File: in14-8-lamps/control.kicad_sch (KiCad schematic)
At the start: 20 parts, among them J2 Conn_01x02_Pin, J3 Conn_01x06_Pin, Q10 2N7002, U3 ESP32-WROOM-32D, U4 DS3231M, U5 74141

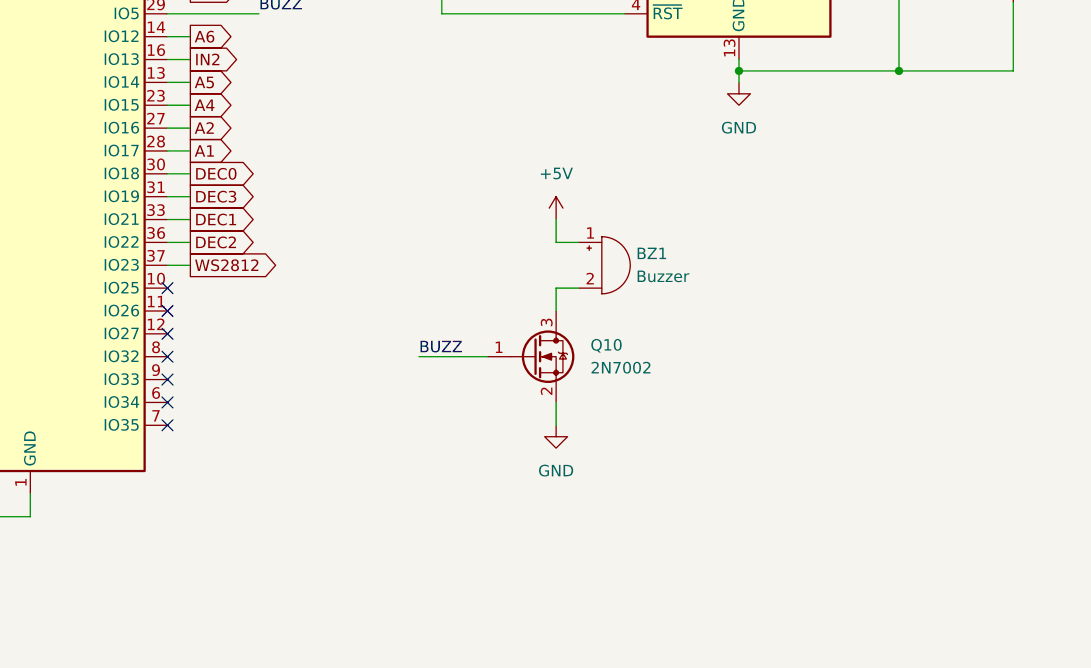
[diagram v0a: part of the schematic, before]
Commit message: add button and ws2812 connector
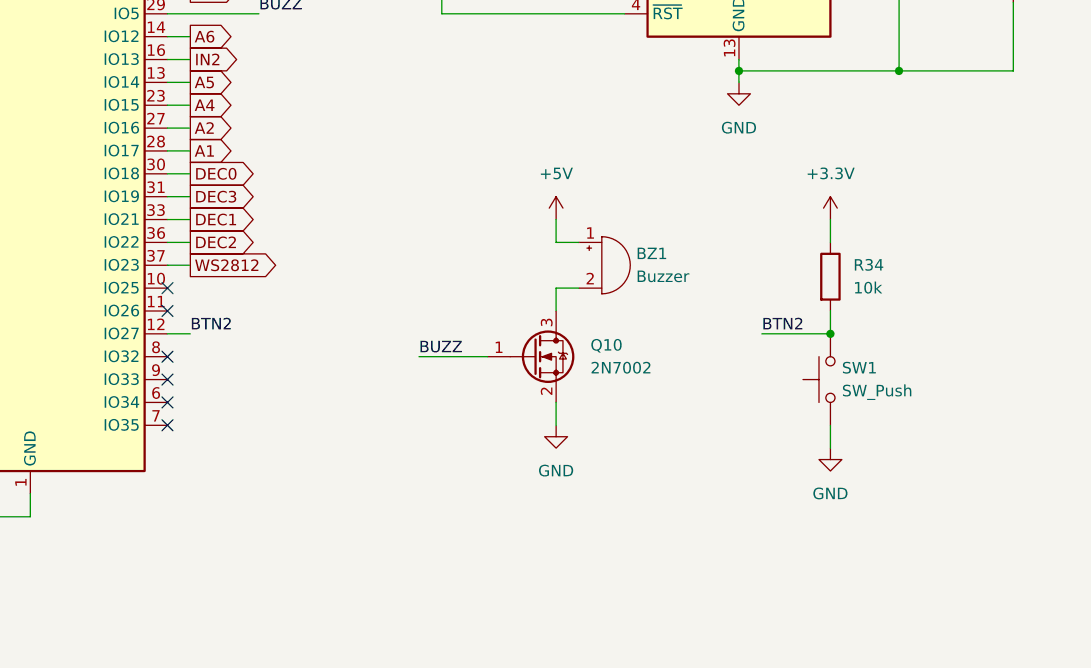
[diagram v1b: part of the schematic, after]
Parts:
- added R34: 10k, Resistor_SMD:R_0805_2012Metric_Pad1.20x1.40mm_HandSolder, symbol Device:R
- added SW1: SW_Push, Button_Switch_SMD:SW_Push_1P1T_NO_6x6mm_H9.5mm, symbol Switch:SW_Push
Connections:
- net +3.3V: now also R34.1
- net GND: now also SW1.1
- net BTN2: now reaches U3.12 (IO27)
- net BTN2: now also R34.2, SW1.2
- no-connect marks 15 -> 14
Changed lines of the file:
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@@
 (kicad_sch (version 20230121) (generator eeschema)
   (paper "A4")
+  (junction (at 152.4 91.44) (diameter 0) (color 0 0 0 0)
+  )
   (junction (at 139.7 30.48) (diameter 0) (color 0 0 0 0)
   )
@@
   (no_connect (at 48.26 81.28))
   (no_connect (at 78.74 101.6))
-  (no_connect (at 78.74 91.44))
   (no_connect (at 78.74 88.9))
   (no_connect (at 78.74 93.98))
@@
     (stroke (width 0) (type default))
   )
+  (wire (pts (xy 152.4 88.9) (xy 152.4 91.44))
+    (stroke (width 0) (type default))
+  )
   (wire (pts (xy 251.46 60.96) (xy 254 60.96))
     (stroke (width 0) (type default))
@@
     (stroke (width 0) (type default))
   )
+  (wire (pts (xy 152.4 78.74) (xy 152.4 81.28))
+    (stroke (width 0) (type default))
+  )
   (wire (pts (xy 118.11 30.48) (xy 118.11 33.02))
     (stroke (width 0) (type default))
@@
     (stroke (width 0) (type default))
   )
+  (wire (pts (xy 144.78 91.44) (xy 152.4 91.44))
+    (stroke (width 0) (type default))
+  )
   (wire (pts (xy 78.74 83.82) (xy 81.28 83.82))
     (stroke (width 0) (type default))
@@
     (stroke (width 0) (type default))
   )
+  (wire (pts (xy 78.74 91.44) (xy 81.28 91.44))
+    (stroke (width 0) (type default))
+  )
   (wire (pts (xy 160.02 40.64) (xy 160.02 62.23))
     (stroke (width 0) (type default))
@@
     (stroke (width 0) (type default))
   )
+  (wire (pts (xy 152.4 101.6) (xy 152.4 104.14))
+    (stroke (width 0) (type default))
+  )
   (wire (pts (xy 78.74 68.58) (xy 81.28 68.58))
     (stroke (width 0) (type default))
@@
     (effects (font (size 1.27 1.27)) (justify left bottom))
   )
+  (label "BTN2" (at 81.28 91.44 0) (fields_autoplaced)
+    (effects (font (size 1.27 1.27)) (justify left bottom))
+  )
   (label "TX" (at 97.79 45.72 0) (fields_autoplaced)
+    (effects (font (size 1.27 1.27)) (justify left bottom))
+  )
+  (label "BTN2" (at 144.78 91.44 0) (fields_autoplaced)
     (effects (font (size 1.27 1.27)) (justify left bottom))
   )
@@
     (property "Intersheetrefs" "${INTERSHEET_REFS}" (at 195.3163 71.12 0)
       (effects (font (size 1.27 1.27)) (justify right) hide)
+    )
+  )
+  (symbol (lib_id "Device:R") (at 152.4 85.09 0) (unit 1)
+    (in_bom yes) (on_board yes) (dnp no) (fields_autoplaced)
+    (property "Reference" "R34" (at 154.94 83.82 0)
+      (effects (font (size 1.27 1.27)) (justify left))
+    )
+    (property "Value" "10k" (at 154.94 86.36 0)
+      (effects (font (size 1.27 1.27)) (justify left))
+    )
+    (property "Footprint" "Resistor_SMD:R_0805_2012Metric_Pad1.20x1.40mm_HandSolder" (at 150.622 85.09 90)
+      (effects (font (size 1.27 1.27)) hide)
+    )
+    (property "Datasheet" "~" (at 152.4 85.09 0)
+      (effects (font (size 1.27 1.27)) hide)
+    )
+    (pin "1")
+    (pin "2")
+    (instances
+      (project "nixie-clock-esp-32"
+        (path "/cd8918ee-e986-4b1b-bef5-f32ed2eef1b1/6a0f8bd2-47e1-46cc-b2ff-e288ea213239"
+          (reference "R34") (unit 1)
+        )
+      )
     )
   )
@@
     )
   )
+  (symbol (lib_id "power:GND") (at 152.4 104.14 0) (unit 1)
+    (in_bom yes) (on_board yes) (dnp no) (fields_autoplaced)
+    (property "Reference" "#PWR027" (at 152.4 110.49 0)
+      (effects (font (size 1.27 1.27)) hide)
+    )
+    (property "Value" "GND" (at 152.4 109.22 0)
+      (effects (font (size 1.27 1.27)))
+    )
+    (property "Footprint" "" (at 152.4 104.14 0)
+      (effects (font (size 1.27 1.27)) hide)
+    )
+    (property "Datasheet" "" (at 152.4 104.14 0)
+      (effects (font (size 1.27 1.27)) hide)
+    )
+    (pin "1")
+    (instances
+      (project "nixie-clock-esp-32"
+        (path "/cd8918ee-e986-4b1b-bef5-f32ed2eef1b1/6a0f8bd2-47e1-46cc-b2ff-e288ea213239"
+          (reference "#PWR027") (unit 1)
+        )
+      )
+    )
+  )
+  (symbol (lib_id "Switch:SW_Push") (at 152.4 96.52 90) (unit 1)
+    (in_bom yes) (on_board yes) (dnp no) (fields_autoplaced)
+    (property "Reference" "SW1" (at 153.67 95.25 90)
+      (effects (font (size 1.27 1.27)) (justify right))
+    )
+    (property "Value" "SW_Push" (at 153.67 97.79 90)
+      (effects (font (size 1.27 1.27)) (justify right))
+    )
+    (property "Footprint" "Button_Switch_SMD:SW_Push_1P1T_NO_6x6mm_H9.5mm" (at 147.32 96.52 0)
+      (effects (font (size 1.27 1.27)) hide)
+    )
+    (property "Datasheet" "~" (at 147.32 96.52 0)
+      (effects (font (size 1.27 1.27)) hide)
+    )
+    (pin "2")
+    (pin "1")
+    (instances
+      (project "nixie-clock-esp-32"
+        (path "/cd8918ee-e986-4b1b-bef5-f32ed2eef1b1/6a0f8bd2-47e1-46cc-b2ff-e288ea213239"
+          (reference "SW1") (unit 1)
+        )
+      )
+    )
+  )
   (symbol (lib_id "Timer_RTC:DS3231M") (at 142.24 50.8 0) (unit 1)
     (in_bom yes) (on_board yes) (dnp no)
@@
         )
       )
+    )
+  )
+  (symbol (lib_id "power:+3.3V") (at 152.4 78.74 0) (unit 1)
+    (in_bom yes) (on_board yes) (dnp no) (fields_autoplaced)
+    (property "Reference" "#PWR022" (at 152.4 82.55 0)
+      (effects (font (size 1.27 1.27)) hide)
+    )
+    (property "Value" "+3.3V" (at 152.4 73.66 0)
+      (effects (font (size 1.27 1.27)))
+    )
+    (property "Footprint" "" (at 152.4 78.74 0)
+      (effects (font (size 1.27 1.27)) hide)
+    )
+    (property "Datasheet" "" (at 152.4 78.74 0)
+      (effects (font (size 1.27 1.27)) hide)
+    )
+    (pin "1")
+    (instances
+      (project "nixie-clock-esp-32"
+        (path "/cd8918ee-e986-4b1b-bef5-f32ed2eef1b1/6a0f8bd2-47e1-46cc-b2ff-e288ea213239"
+          (reference "#PWR022") (unit 1)
+        )
+      )
